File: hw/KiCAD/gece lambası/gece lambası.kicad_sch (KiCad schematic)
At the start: 4 parts, among them J1 Analog, J2 Digital

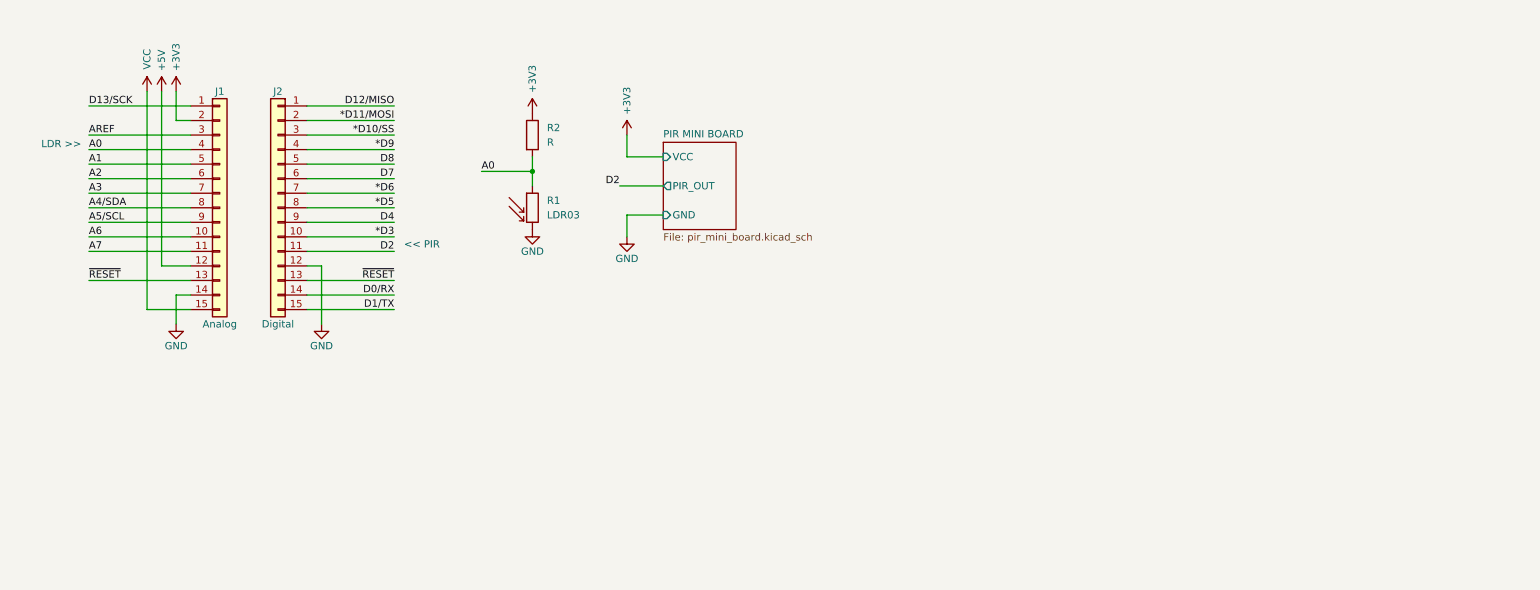
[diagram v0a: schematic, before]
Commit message: 2. ders sonrasında proje şematiği güncellendi. Devre simülasyonu ve test frimware yazılımları yazıldı
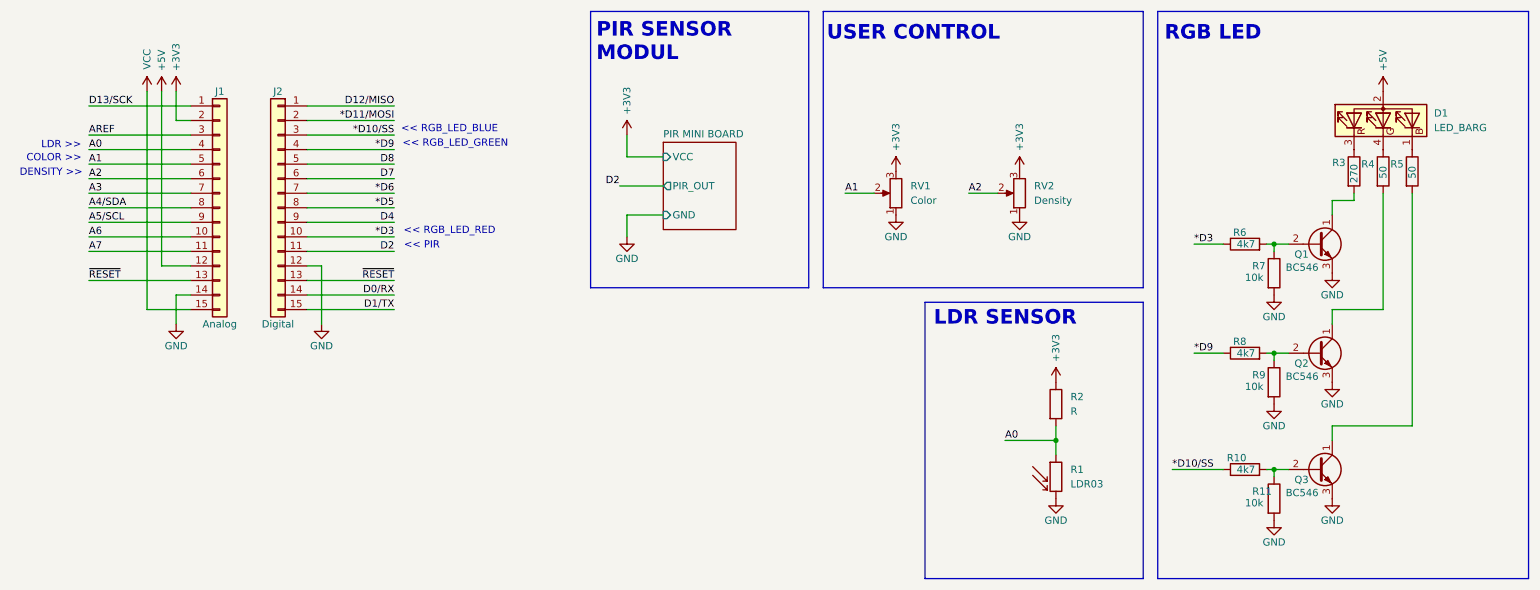
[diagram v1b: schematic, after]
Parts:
- added D1: LED_BARG, symbol Device:LED_BARG
- added Q1, Q2, Q3: BC546, Package_TO_SOT_THT:TO-92_Inline, symbol Transistor_BJT:BC546
- added R10, R6, R8: 4k7, symbol Device:R
- added R11, R7, R9: 10k, symbol Device:R
- added R3: 270, symbol Device:R
- added R4, R5: 50, symbol Device:R
- added RV1: Color, symbol Device:R_Potentiometer
- added RV2: Density, symbol Device:R_Potentiometer
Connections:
- net *D10/SS: now also R10.1
- net *D3: now also R6.1
- net *D9: now also R8.1
- net +3V3: now also RV1.3, RV2.3
- net +5V: now also D1.2 (A)
- net A1: now also RV1.2
- net A2: now also RV2.2
- net GND: now also Q1.3 (E), Q2.3 (E), Q3.3 (E), R11.2, R7.2, R9.2, RV1.1, RV2.1
- new net: Q2.1 (C), R4.2
- new net: Q2.2 (B), R8.2, R9.1
- new net: D1.1 (BK), R5.1
- new net: Q3.1 (C), R5.2
- new net: D1.3 (RK), R3.1
- new net: D1.4 (GK), R4.1
- new net: Q3.2 (B), R10.2, R11.1
- new net: Q1.2 (B), R6.2, R7.1
- new net: Q1.1 (C), R3.2
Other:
- note added: "<< RGB_LED_BLUE"
- note added: "<< RGB_LED_GREEN"
- note added: "<< RGB_LED_RED"
- note added: "COLOR >>"
- note added: "DENSITY >>"
- note added: "LDR SENSOR"
- note added: "PIR SENSOR MODUL"
- note added: "RGB LED"
- note added: "USER CONTROL"
- moved on the sheet: R1, R2

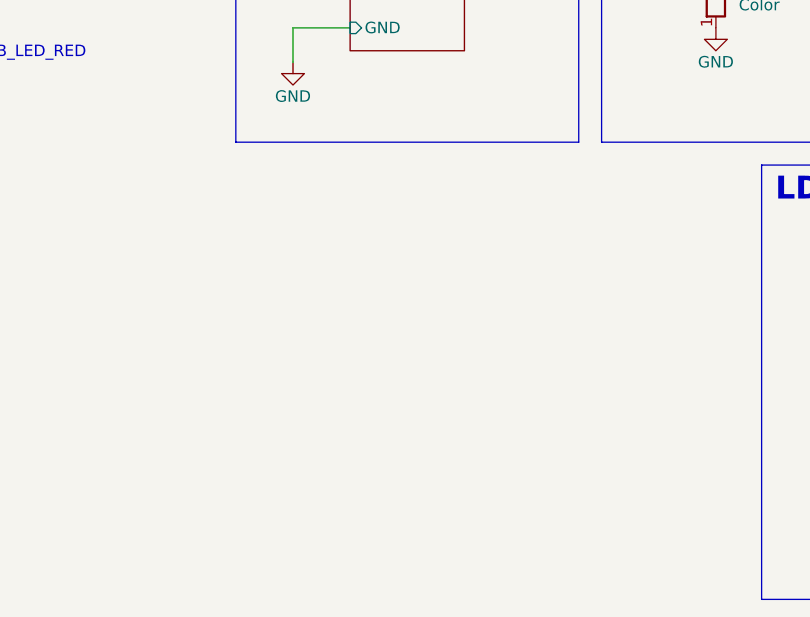
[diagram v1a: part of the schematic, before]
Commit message: Proje açıklama kısmı güncellendi. Şematik çizimine güç girişi eklendi.
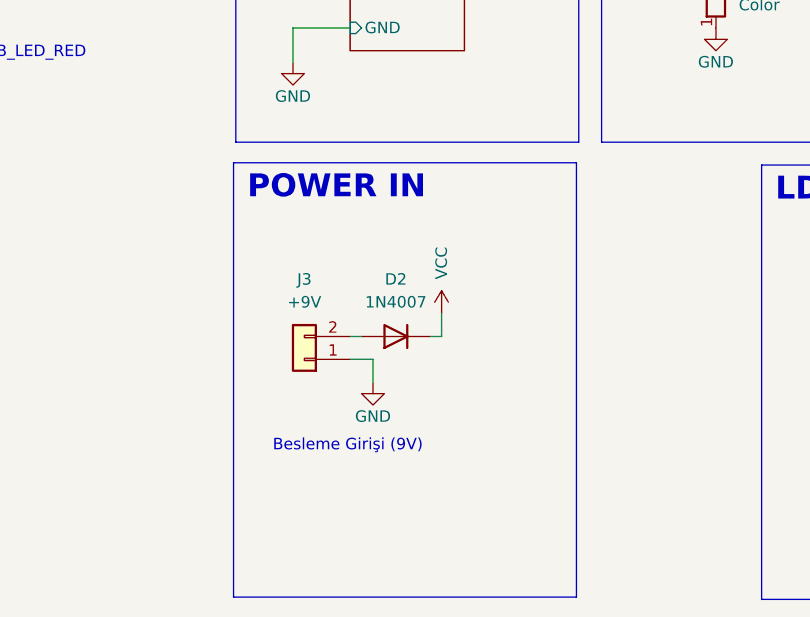
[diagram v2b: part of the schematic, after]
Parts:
- added D2: 1N4007, Diode_THT:D_DO-41_SOD81_P10.16mm_Horizontal, symbol Diode:1N4007
- added J3: +9V, symbol Connector_Generic:Conn_01x02
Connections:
- net GND: now also J3.1 (Pin_1)
- net VCC: now also D2.1 (K)
- new net: D2.2 (A), J3.2 (Pin_2)
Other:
- note added: "Besleme Girişi (9V)"
- note added: "POWER IN"
